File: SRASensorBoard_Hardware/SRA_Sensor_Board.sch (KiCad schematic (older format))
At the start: 70 parts, among them J1 USB_B_Micro, Q1 CSD17305Q5A, U1 LM3478MMX_NOPB, U2 OKI, U3 OKI, U4 TM4C129E_Launchpad, U5 MAX232, U6 IRF7821PbF

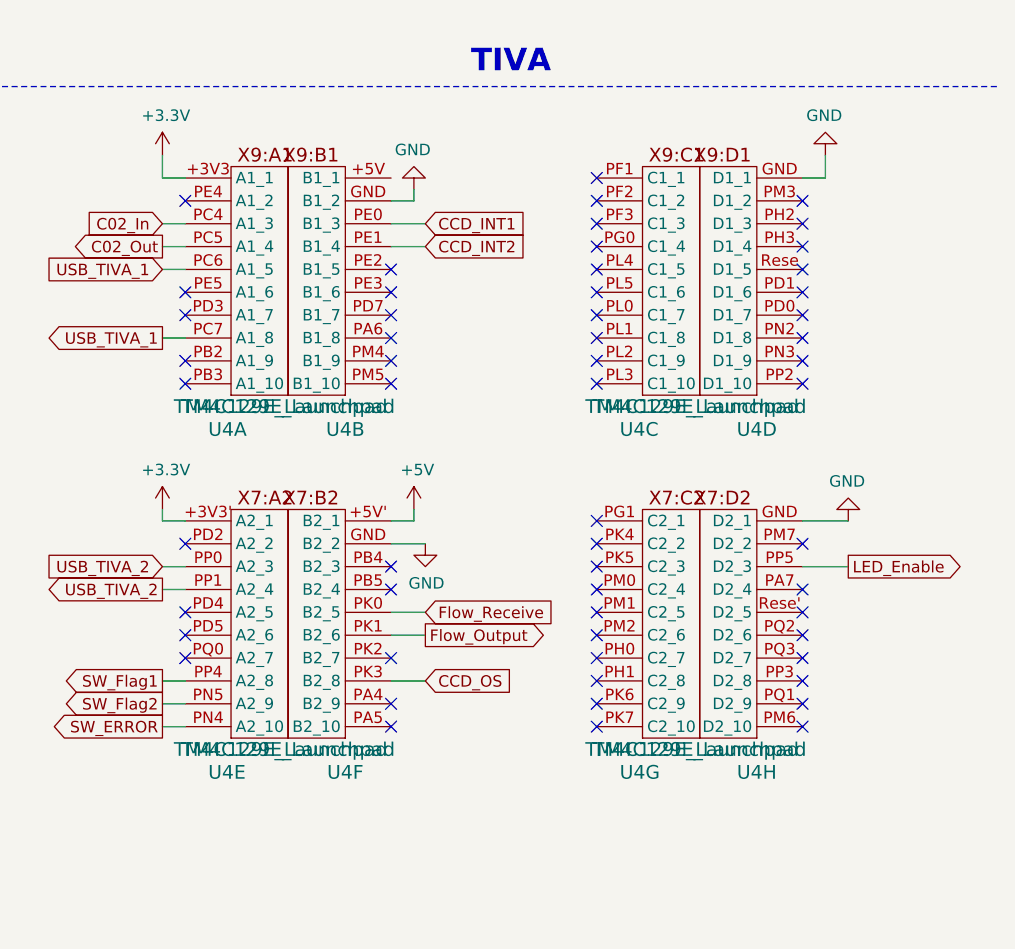
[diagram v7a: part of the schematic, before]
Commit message: Board Update
Layout is done. All traces are done. LEDs are done.
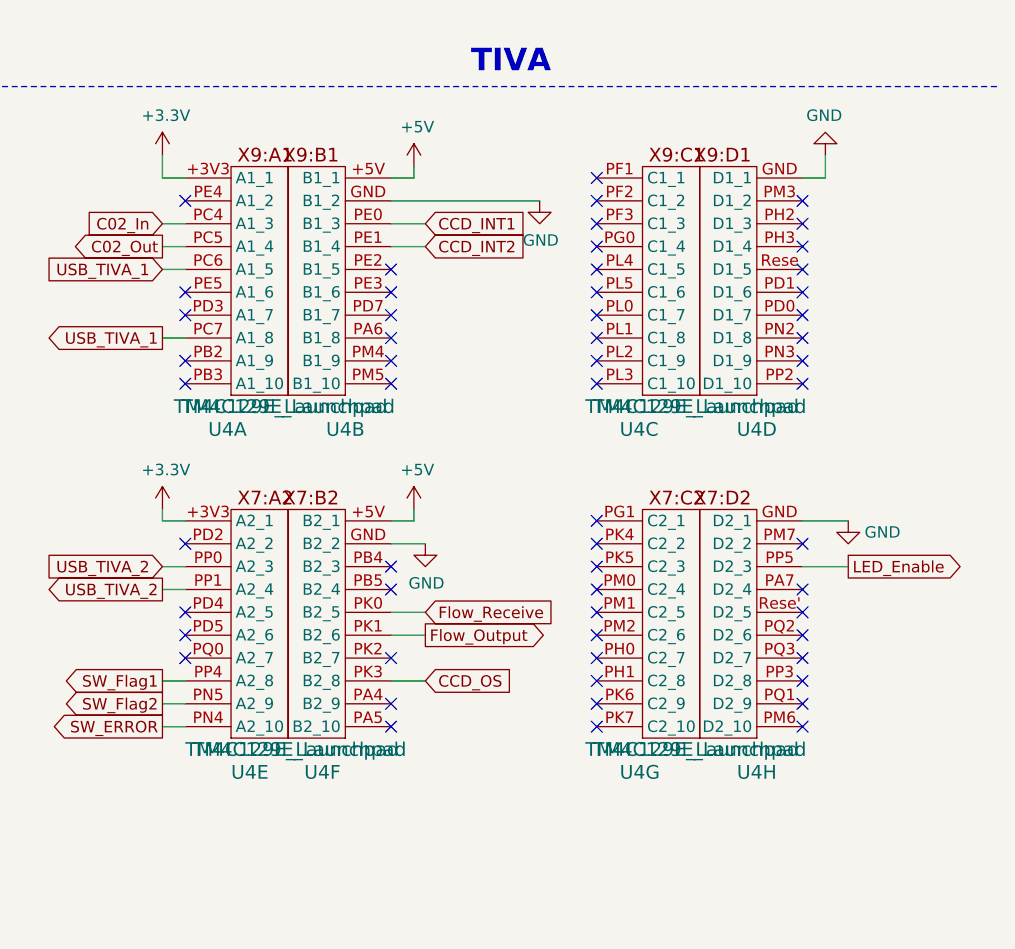
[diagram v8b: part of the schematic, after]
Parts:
- removed unit 5 of U4
- removed unit 6 of U4
- added unit 6 of U4
- added unit 5 of U4
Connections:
- net +3V3: now also U4.+3V3 (A2_1)
- net +5V: now also U4.+5V (B1_1), U4.+5V (B2_1)
- net CCD_OS: now also U4.PK3 (B2_8)
- net Flow_Output: now also U4.PK1 (B2_6)
- net Flow_Receive: now also U4.PK0 (B2_5)
- net GND: now also U4.GND (B2_2)
- net SW_ERROR: now also U4.PN4 (A2_10)
- net SW_Flag1: now also U4.PP4 (A2_8)
- net SW_Flag2: now also U4.PN5 (A2_9)
- net USB_TIVA_2: now also U4.PP0 (A2_3), U4.PP1 (A2_4)
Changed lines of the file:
@@
 P 15450 2650
 F 0 "#PWR025" H 15450 2400 50  0001 C CNN
-F 1 "GND" H 15455 2477 50  0000 C CNN
+F 1 "GND" H 15600 2600 50  0000 C CNN
 F 2 "" H 15450 2650 50  0001 C CNN
 F 3 "" H 15450 2650 50  0001 C CNN
 	1    15450 2650
-	-1   0    0    1
+	1    0    0    -1
 $EndComp
 Wire Wire Line
@@
 Text GLabel 13600 3350 2    50   Input ~ 0
 CCD_OS
-Wire Wire Line
-	12450 3550 12550 3550
 Text GLabel 12450 3550 0    50   Output ~ 0
 SW_ERROR
-Wire Wire Line
-	12450 3450 12550 3450
 Text GLabel 12450 3450 0    50   Output ~ 0
 SW_Flag2
-Wire Wire Line
-	12450 3350 12550 3350
 Text GLabel 12450 3350 0    50   Output ~ 0
 SW_Flag1
@@
 Text GLabel 13600 1350 2    50   Input ~ 0
 CCD_INT1
-Wire Wire Line
-	13550 1250 13450 1250
-Wire Wire Line
-	13550 1250 13550 1200
 $Comp
 L power:GND #PWR021
 U 1 1 5DA35372
-P 13550 1200
-F 0 "#PWR021" H 13550 950 50  0001 C CNN
-F 1 "GND" H 13555 1027 50  0000 C CNN
-F 2 "" H 13550 1200 50  0001 C CNN
-F 3 "" H 13550 1200 50  0001 C CNN
-	1    13550 1200
-	-1   0    0    1
+P 14100 1250
+F 0 "#PWR021" H 14100 1000 50  0001 C CNN
+F 1 "GND" H 14105 1077 50  0000 C CNN
+F 2 "" H 14100 1250 50  0001 C CNN
+F 3 "" H 14100 1250 50  0001 C CNN
+	1    14100 1250
+	1    0    0    -1
 $EndComp
 Wire Wire Line
@@
 Text Notes 10850 7850 0    98   ~ 20
 Indicators
-NoConn ~ 12550 2750
 $Comp
 L power:+24V #PWR016
@@
 	1    0    0    -1
 $EndComp
-NoConn ~ 12550 3250
-NoConn ~ 12550 3150
-NoConn ~ 12550 3050
 NoConn ~ 13450 2850
 NoConn ~ 13450 2950
@@
 Wire Wire Line
 	12450 2600 12450 2650
-Wire Wire Line
-	12450 2650 12550 2650
-$Comp
-L power:+5V #PWR022
-U 1 1 5DC1A2BD
-P 13550 2600
-F 0 "#PWR022" H 13550 2450 50  0001 C CNN
-F 1 "+5V" H 13565 2773 50  0000 C CNN
-F 2 "" H 13550 2600 50  0001 C CNN
-F 3 "" H 13550 2600 50  0001 C CNN
-	1    13550 2600
-	1    0    0    -1
-$EndComp
-Wire Wire Line
-	13550 2600 13550 2650
-Wire Wire Line
-	13550 2650 13450 2650
 $Comp
 L Device:C C9
@@
 Text GLabel 12450 2950 0    50   Output ~ 0
 USB_TIVA_2
-Wire Wire Line
-	12450 2850 12550 2850
-Wire Wire Line
-	12450 2950 12550 2950
 Text GLabel 13600 3050 2    50   Input ~ 0
 Flow_Receive
@@
 	1    12750 2100
 	1    0    0    -1
-$EndComp
-$Comp
-L SRA_Sensor_Board-rescue:TM4C129E_Launchpad-MRDT_Shields-SRA_Sensor_Board-rescue U4
-U 5 1 5DD95673
-P 12750 3600
-F 0 "U4" H 12650 3450 60  0000 L CNN
-F 1 "TM4C129E_Launchpad" H 12500 3550 60  0000 L CNN
-F 2 "MRDT_Shields:TM4C129E_Launchpad_FULL_THT_TOP" H 12750 3600 60  0001 C CNN
-F 3 "" H 12750 3600 60  0001 C CNN
-	5    12750 3600
-	1    0    0    -1
-$EndComp
-$Comp
-L SRA_Sensor_Board-rescue:TM4C129E_Launchpad-MRDT_Shields-SRA_Sensor_Board-rescue U4
-U 6 1 5DD9982E
-P 13250 3600
-F 0 "U4" H 13250 3450 60  0000 C CNN
-F 1 "TM4C129E_Launchpad" H 13500 3550 60  0000 C CNN
-F 2 "MRDT_Shields:TM4C129E_Launchpad_FULL_THT_TOP" H 13250 3600 60  0001 C CNN
-F 3 "" H 13250 3600 60  0001 C CNN
-	6    13250 3600
-	-1   0    0    -1
 $EndComp
 $Comp
@@
 Wire Wire Line
 	7950 9100 7950 9450
+NoConn ~ 12550 3250
+Wire Wire Line
+	12450 3350 12550 3350
+Wire Wire Line
+	12450 2950 12550 2950
+Wire Wire Line
+	12450 2850 12550 2850
+Wire Wire Line
+	12450 3450 12550 3450
+Wire Wire Line
+	12450 3550 12550 3550
+NoConn ~ 12550 3150
+NoConn ~ 12550 3050
+NoConn ~ 12550 2750
+Wire Wire Line
+	12450 2650 12550 2650
+$Comp
+L MRDT_Shields:TM4C129E_Launchpad U4
+U 5 1 5DD6BB3C
+P 12750 3600
+F 0 "U4" H 12750 3450 60  0000 L CNN
+F 1 "TM4C129E_Launchpad" H 12550 3550 60  0000 L CNN
+F 2 "MRDT_Shields:TM4C129E_Launchpad_FULL_THT_TOP" H 12750 3600 60  0001 C CNN
+F 3 "" H 12750 3600 60  0001 C CNN
+	5    12750 3600
+	1    0    0    -1
+$EndComp
+$Comp
+L MRDT_Shields:TM4C129E_Launchpad U4
+U 6 1 5DD2931F
+P 13250 3600
+F 0 "U4" H 13350 3450 60  0000 C CNN
+F 1 "TM4C129E_Launchpad" H 13450 3550 60  0000 C CNN
+F 2 "MRDT_Shields:TM4C129E_Launchpad_FULL_THT_TOP" H 13250 3600 60  0001 C CNN
+F 3 "" H 13250 3600 60  0001 C CNN
+	6    13250 3600
+	-1   0    0    -1
+$EndComp
+Wire Wire Line
+	13550 2650 13450 2650
+Wire Wire Line
+	13550 2600 13550 2650
+$Comp
+L power:+5V #PWR022
+U 1 1 5DC1A2BD
+P 13550 2600
+F 0 "#PWR022" H 13550 2450 50  0001 C CNN
+F 1 "+5V" H 13565 2773 50  0000 C CNN
+F 2 "" H 13550 2600 50  0001 C CNN
+F 3 "" H 13550 2600 50  0001 C CNN
+	1    13550 2600
+	1    0    0    -1
+$EndComp
+Wire Wire Line
+	13550 1150 13450 1150
+Wire Wire Line
+	13550 1100 13550 1150
+$Comp
+L power:+5V #PWR0135
+U 1 1 5DD8CC54
+P 13550 1100
+F 0 "#PWR0135" H 13550 950 50  0001 C CNN
+F 1 "+5V" H 13565 1273 50  0000 C CNN
+F 2 "" H 13550 1100 50  0001 C CNN
+F 3 "" H 13550 1100 50  0001 C CNN
+	1    13550 1100
+	1    0    0    -1
+$EndComp
+Wire Wire Line
+	13450 1250 14100 1250
 $EndSCHEMATC
